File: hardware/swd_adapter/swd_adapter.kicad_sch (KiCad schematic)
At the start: 11 parts, among them J1 FFC_Prog_Conn, J2 Conn_ARM_JTAG_SWD_10, J3 Conn_01x02, J4 Conn_01x08, J5 Conn_01x03, SW1 SW_Slide_DPDT

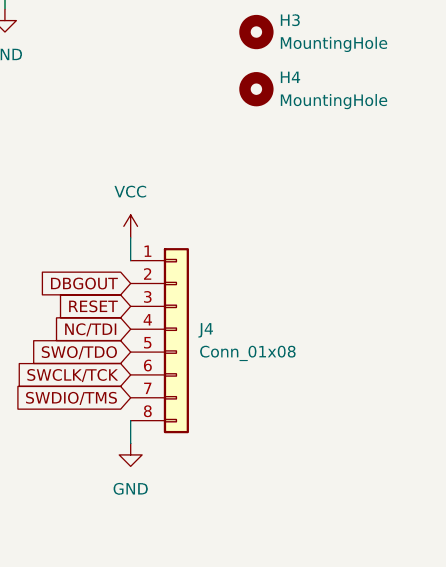
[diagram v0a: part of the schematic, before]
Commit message: Changed LEDs module to use FIFO and got UART for logging working
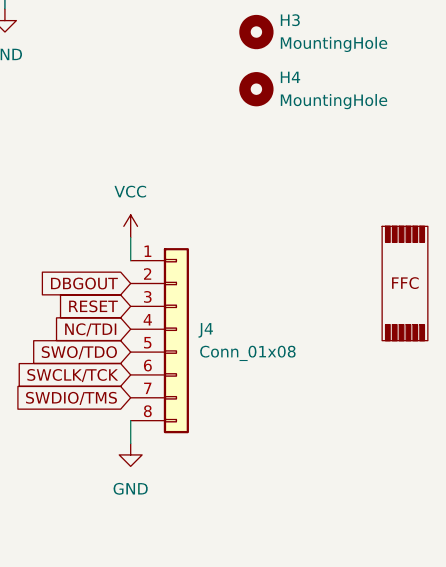
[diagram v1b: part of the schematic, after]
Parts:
- added M1: ~, symbol KiPLM:CBL/CBL-0000-0092
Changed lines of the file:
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@@
+	)
+	(symbol
+		(lib_id "KiPLM:CBL/CBL-0000-0092")
+		(at 195.58 83.82 0)
+		(unit 1)
+		(exclude_from_sim no)
+		(in_bom yes)
+		(on_board no)
+		(dnp no)
+		(fields_autoplaced yes)
+		(property "Reference" "M1"
+			(at 195.58 83.82 0)
+			(effects
+				(font
+					(size 1.27 1.27)
+				)
+				(hide yes)
+			)
+		)
+		(property "Value" "~"
+			(at 199.39 83.82 0)
+			(effects
+				(font
+					(size 1.27 1.27)
+				)
+				(justify left)
+			)
+		)
+		(property "Footprint" ""
+			(at 195.58 83.82 0)
+			(effects
+				(font
+					(size 1.27 1.27)
+				)
+				(hide yes)
+			)
+		)
+		(property "Datasheet" "https://www.molex.com/en-us/products/part-detail/151200092?display=pdf"
+			(at 195.58 83.82 0)
+			(effects
+				(font
+					(size 1.27 1.27)
+				)
+				(hide yes)
+			)
+		)
+		(property "Description" "FFC / FPC Jumper Cables 0.50mm Ptch Jumper Opp Side Contacts (Type D) 254mm Lngth  (Au) Plating 8 Ckts"
+			(at 195.58 83.82 0)
+			(effects
+				(font
+					(size 1.27 1.27)
+				)
+				(hide yes)
+			)
+		)
+		(property "IPN" "CBL-0000-0092"
+			(at 195.58 83.82 0)
+			(effects
+				(font
+					(size 1.27 1.27)
+				)
+				(hide yes)
+			)
+		)
+		(property "MPN" "15120-0092"
+			(at 195.58 83.82 0)
+			(effects
+				(font
+					(size 1.27 1.27)
+				)
+				(hide yes)
+			)
+		)
+		(property "Manufacturer" "Molex"
+			(at 195.58 83.82 0)
+			(effects
+				(font
+					(size 1.27 1.27)
+				)
+				(hide yes)
+			)
+		)
+		(property "Symbol" "KiPLM_Symbols:Flat_Flex_Cable"
+			(at 195.58 83.82 0)
+			(effects
+				(font
+					(size 1.27 1.27)
+				)
+				(hide yes)
+			)
+		)
+		(property "Mouser-PN" "538-15120-0092"
+			(at 195.58 83.82 0)
+			(effects
+				(font
+					(size 1.27 1.27)
+				)
+				(hide yes)
+			)
+		)
+		(property "DigiKey-PN" ""
+			(at 195.58 83.82 0)
+			(effects
+				(font
+					(size 1.27 1.27)
+				)
+				(hide yes)
+			)
+		)
+		(instances
+			(project ""
+				(path "/9858ffad-0124-4064-9390-4cd0caa8fd61"
+					(reference "M1")
+					(unit 1)
+				)
+			)
+		)
 	)
 	(symbol
